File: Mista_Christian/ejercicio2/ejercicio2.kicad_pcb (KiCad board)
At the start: 2 copper layers, 40.6 x 61 mm, 13 parts, among them J1 DB9, U1 AMIS42665TJAA1RG, U2 SSS232V1

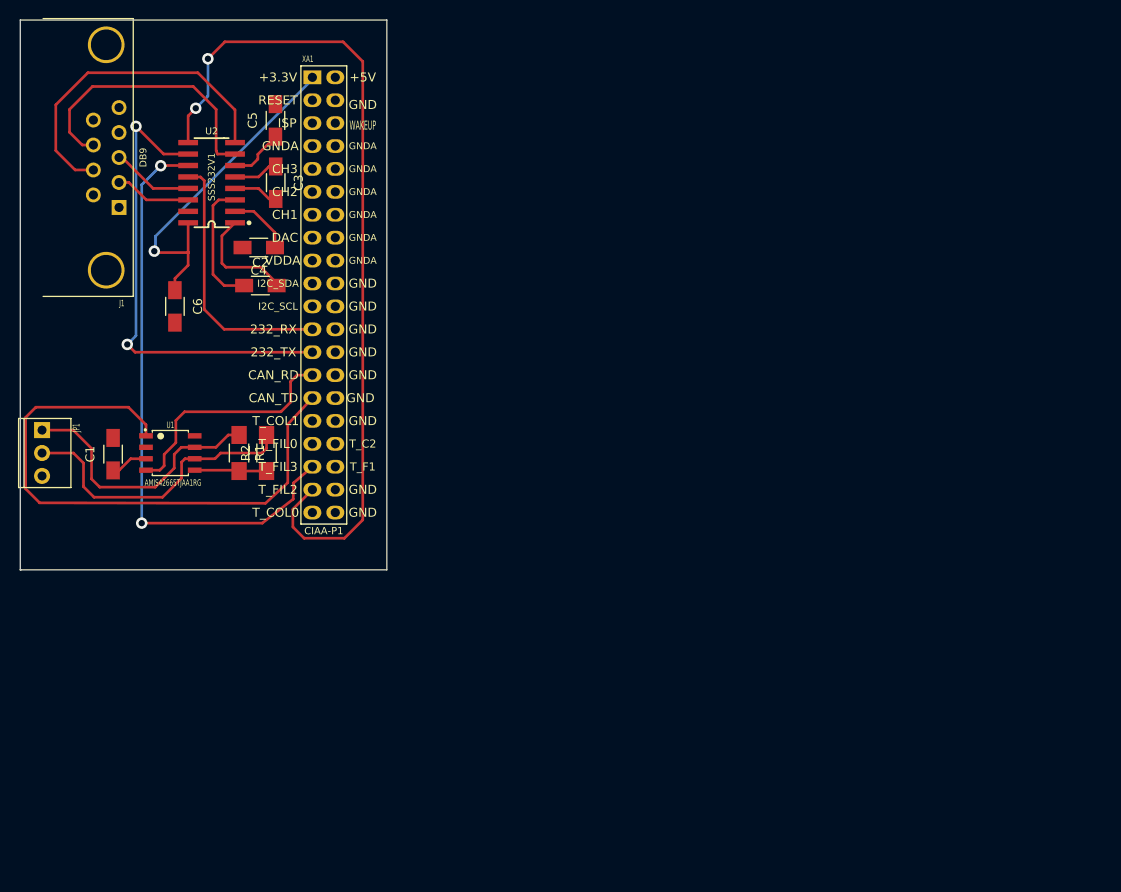
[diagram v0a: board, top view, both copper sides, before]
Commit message: 3D routing
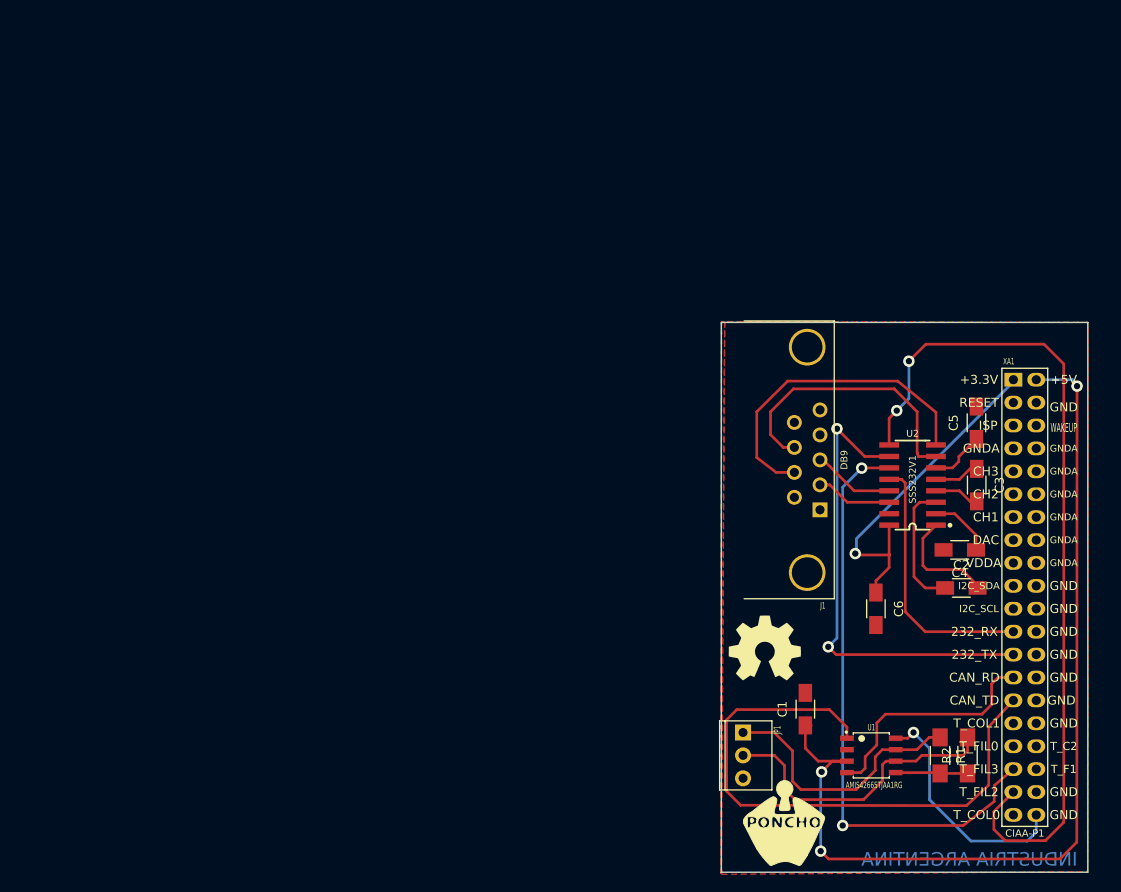
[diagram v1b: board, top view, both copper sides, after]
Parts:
- added G***: LOGO, ej2:Logo_Poncho, F.Cu at (143.2, 131.0)
- added G101: Logo_OSHWA, ej2:Logo_OSHWA, F.Cu at (141.1, 111.5)
- moved C3 84.6 mm to (164.6, 93.5)
- moved C4 84.6 mm to (162.7, 100.7)
- moved C6 84.6 mm to (153.4, 107.2)
- moved XA1 84.6 mm to (168.7, 81.8)
- moved C2 84.6 mm to (162.9, 104.9)
- moved C5 84.6 mm to (164.6, 86.6)
- moved J1 84.6 mm to (145.8, 90.7)
- moved JP1 84.6 mm to (138.7, 123.4)
- moved R1 84.6 mm to (160.5, 123.4)
- moved R2 84.6 mm to (163.6, 123.4)
- moved U1 84.6 mm to (152.9, 123.4)
- moved U2 84.6 mm to (157.5, 93.5)
- moved C1 81.8 mm to (145.6, 118.3)
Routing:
- net +5V: track 4.33 -> 105.7 mm, vias 0 -> 3
- net GND: track 0.00 -> 26.5 mm, vias 0 -> 1
- net Net-(J1-Pad7): track 36.8 -> 35.9 mm
- added copper zone on B.Cu, net GND
- added copper zone on F.Cu, net GND
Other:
- board text added: "INDUSTRIA ARGENTINA"
